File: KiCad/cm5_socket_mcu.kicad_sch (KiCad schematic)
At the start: 3 parts, among them IC1 AZ1117CH2-3.3TRG1

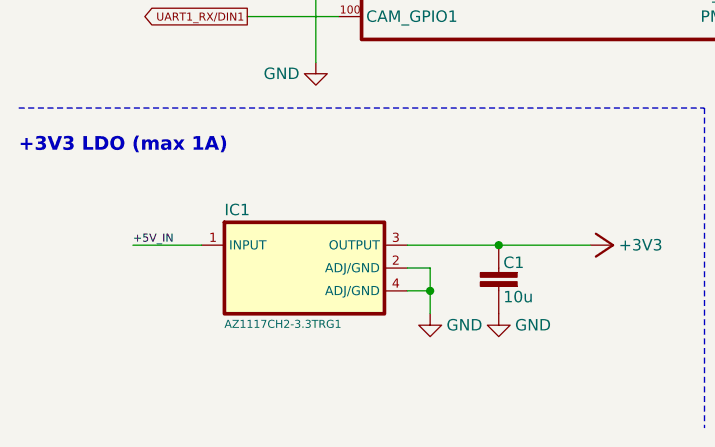
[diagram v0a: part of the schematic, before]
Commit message: Folders paths adjusted, Cin added to 3V3 LDO
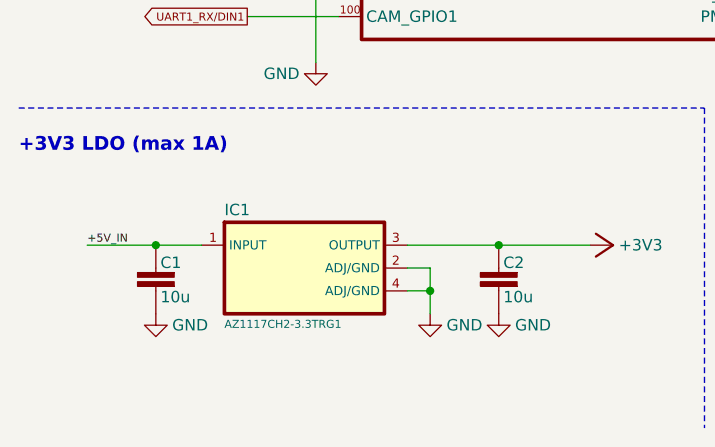
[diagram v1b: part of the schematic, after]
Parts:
- added C1: 10u, PCM_EEZ_passives:C_0603_1608Metric, symbol PCM_EEZ_passives:C-EU
- renumbered C1 to C2
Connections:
- net +5V_IN: now also C1.2
- net GND: now also C1.1
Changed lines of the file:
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@@
 	(title_block
 		(title "${project_name}")
-		(date "2025-11-02")
+		(date "2025-11-03")
 		(rev "${project_version}")
 		(company "${project_creator}")

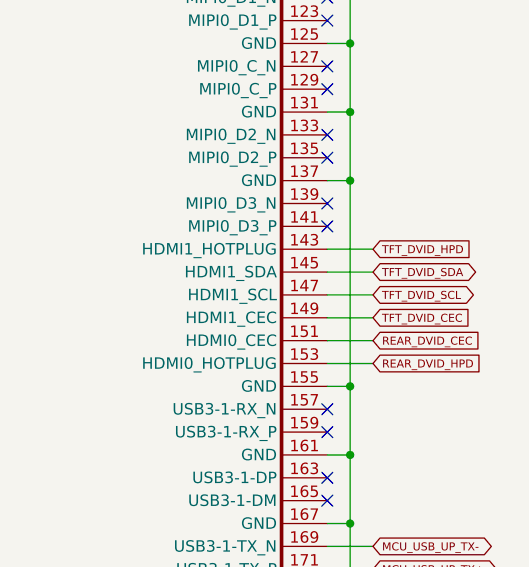
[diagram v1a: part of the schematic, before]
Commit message: TFT_DVID control signals on 1:2 video mux removed
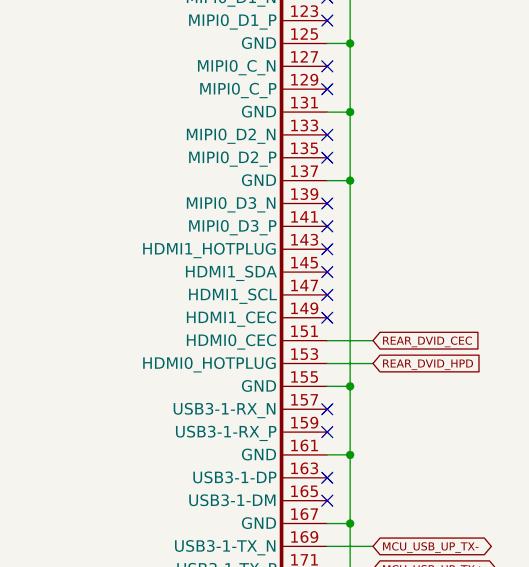
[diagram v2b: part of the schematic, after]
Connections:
- net TFT_DVID_CEC: no longer names the net of SoM1.149 (HDMI1_CEC)
- net TFT_DVID_HPD: no longer names the net of SoM1.143 (HDMI1_HOTPLUG)
- net TFT_DVID_SCL: no longer names the net of SoM1.147 (HDMI1_SCL)
- net TFT_DVID_SDA: no longer names the net of SoM1.145 (HDMI1_SDA)
- no-connect marks 67 -> 71
